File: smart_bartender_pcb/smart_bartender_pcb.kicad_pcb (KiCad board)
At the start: 2 copper layers, 105 x 60 mm, 8 parts, among them J1 Screw_Terminal_01x02, U1 AMS1117-5.0, U2 ULN2803A

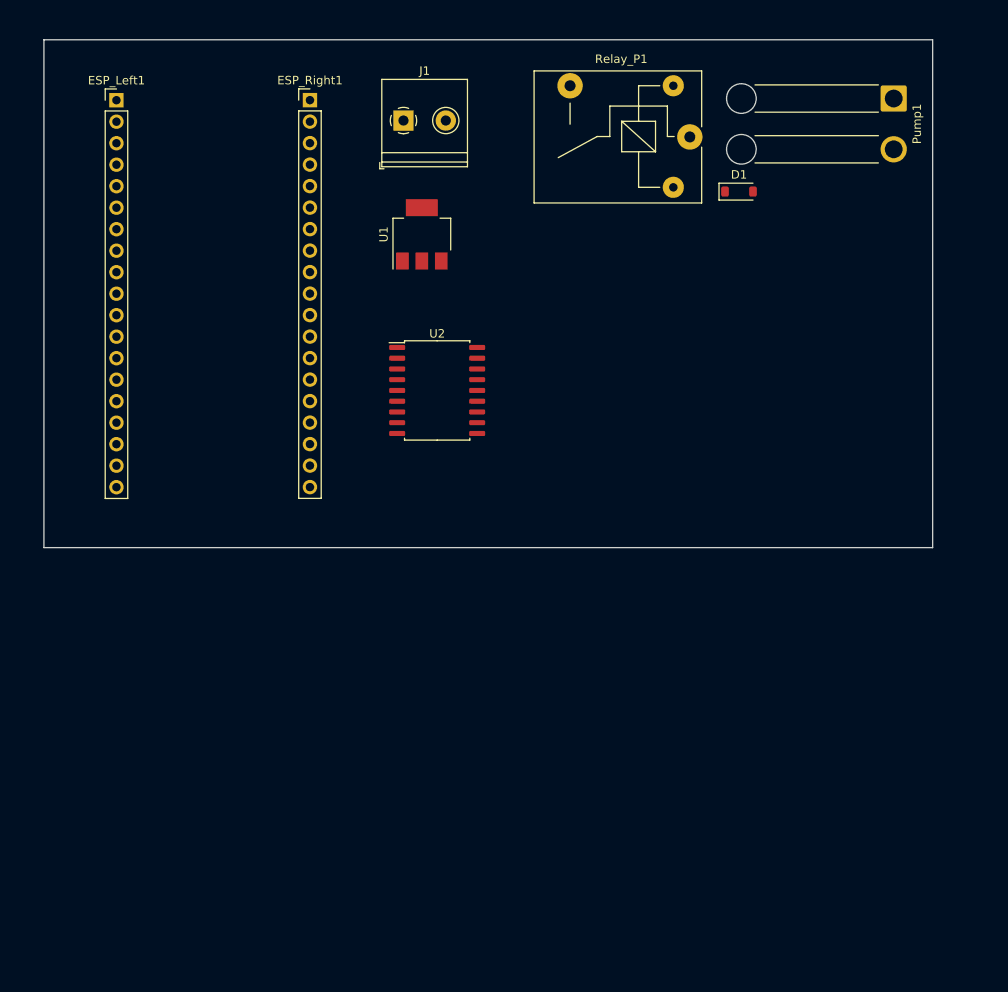
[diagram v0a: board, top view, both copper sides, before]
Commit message: started pcb layout
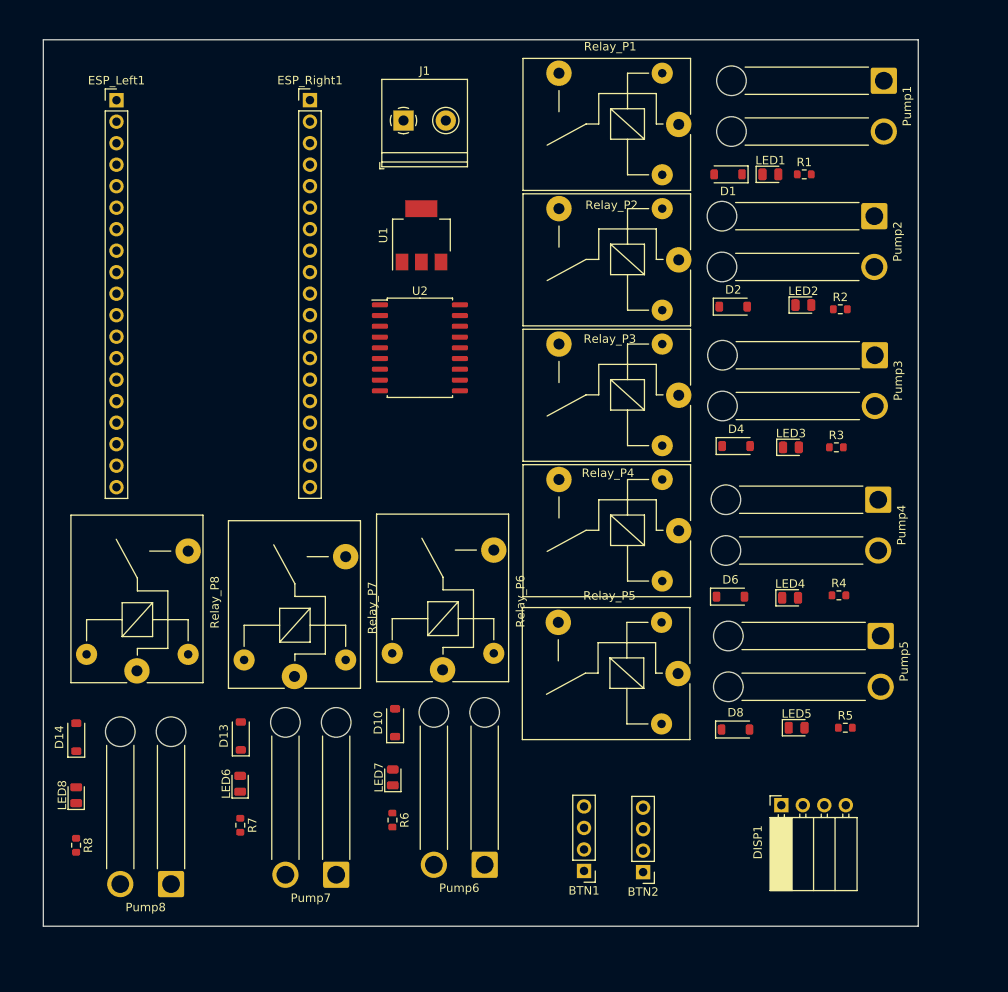
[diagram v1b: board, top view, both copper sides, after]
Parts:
- added BTN1: SW_Push_LED, Connector_PinHeader_2.54mm:PinHeader_1x04_P2.54mm_Vertical, F.Cu at (93.8, 118.2)
- added BTN2: SW_Push_LED, Connector_PinHeader_2.54mm:PinHeader_1x04_P2.54mm_Vertical, F.Cu at (100.8, 118.3)
- added D10: 1N4007, Diode_SMD:D_SOD-123, F.Cu at (71.5, 100.7)
- added D13: 1N4007, Diode_SMD:D_SOD-123, F.Cu at (53.3, 102.2)
- added D14: 1N4007, Diode_SMD:D_SOD-123, F.Cu at (33.8, 102.4)
- added D2: 1N4007, Diode_SMD:D_SOD-123, F.Cu at (111.4, 51.5)
- added D4: 1N4007, Diode_SMD:D_SOD-123, F.Cu at (111.8, 68.0)
- added D6: 1N4007, Diode_SMD:D_SOD-123, F.Cu at (111.1, 85.8)
- added D8: 1N4007, Diode_SMD:D_SOD-123, F.Cu at (111.7, 101.5)
- added DISP1: ~, Connector_PinSocket_2.54mm:PinSocket_1x04_P2.54mm_Horizontal, F.Cu at (117.1, 110.4)
- added LED1: LED, LED_SMD:LED_0805_2012Metric, F.Cu at (115.8, 35.9)
- added LED2: LED, LED_SMD:LED_0805_2012Metric, F.Cu at (119.7, 51.3)
- added LED3: LED, LED_SMD:LED_0805_2012Metric, F.Cu at (118.3, 68.2)
- added LED4: LED, LED_SMD:LED_0805_2012Metric, F.Cu at (118.2, 85.9)
- added LED5: LED, LED_SMD:LED_0805_2012Metric, F.Cu at (118.9, 101.3)
- added LED6: LED, LED_SMD:LED_0805_2012Metric, F.Cu at (53.2, 107.9)
- added LED7: LED, LED_SMD:LED_0805_2012Metric, F.Cu at (71.2, 107.2)
- added LED8: LED, LED_SMD:LED_0805_2012Metric, F.Cu at (33.8, 109.2)
- added Pump2: Conn_01x02_Socket, Connector_Wire:SolderWire-1.5sqmm_1x02_P6mm_D1.7mm_OD3mm_Relief, F.Cu at (128.1, 40.8)
- added Pump3: Conn_01x02_Socket, Connector_Wire:SolderWire-1.5sqmm_1x02_P6mm_D1.7mm_OD3mm_Relief, F.Cu at (128.2, 57.3)
- added Pump4: Conn_01x02_Socket, Connector_Wire:SolderWire-1.5sqmm_1x02_P6mm_D1.7mm_OD3mm_Relief, F.Cu at (128.6, 74.3)
- added Pump5: Conn_01x02_Socket, Connector_Wire:SolderWire-1.5sqmm_1x02_P6mm_D1.7mm_OD3mm_Relief, F.Cu at (128.9, 90.4)
- added Pump6: Conn_01x02_Socket, Connector_Wire:SolderWire-1.5sqmm_1x02_P6mm_D1.7mm_OD3mm_Relief, F.Cu at (82.1, 117.5)
- added Pump7: Conn_01x02_Socket, Connector_Wire:SolderWire-1.5sqmm_1x02_P6mm_D1.7mm_OD3mm_Relief, F.Cu at (64.5, 118.7)
- added Pump8: Conn_01x02_Socket, Connector_Wire:SolderWire-1.5sqmm_1x02_P6mm_D1.7mm_OD3mm_Relief, F.Cu at (45.0, 119.8)
- added R1: 110, Resistor_SMD:R_0603_1608Metric, F.Cu at (119.8, 35.9)
- added R2: 110, Resistor_SMD:R_0603_1608Metric, F.Cu at (124.1, 51.8)
- added R3: 110, Resistor_SMD:R_0603_1608Metric, F.Cu at (123.6, 68.2)
- added R4: 110, Resistor_SMD:R_0603_1608Metric, F.Cu at (123.9, 85.6)
- added R5: 110, Resistor_SMD:R_0603_1608Metric, F.Cu at (124.7, 101.3)
- added R6: 110, Resistor_SMD:R_0603_1608Metric, F.Cu at (71.2, 112.2)
- added R7: 110, Resistor_SMD:R_0603_1608Metric, F.Cu at (53.2, 112.8)
- added R8: 110, Resistor_SMD:R_0603_1608Metric, F.Cu at (33.8, 115.2)
- added Relay_P2: SANYOU_SRD_Form_A, Relay_THT:Relay_SPST_SANYOU_SRD_Series_Form_A, F.Cu at (105.0, 46.0)
- added Relay_P3: SANYOU_SRD_Form_A, Relay_THT:Relay_SPST_SANYOU_SRD_Series_Form_A, F.Cu at (105.0, 62.0)
- added Relay_P4: SANYOU_SRD_Form_A, Relay_THT:Relay_SPST_SANYOU_SRD_Series_Form_A, F.Cu at (105.0, 78.0)
- added Relay_P5: SANYOU_SRD_Form_A, Relay_THT:Relay_SPST_SANYOU_SRD_Series_Form_A, F.Cu at (104.9, 94.9)
- added Relay_P6: SANYOU_SRD_Form_A, Relay_THT:Relay_SPST_SANYOU_SRD_Series_Form_A, F.Cu at (77.1, 94.4)
- added Relay_P7: SANYOU_SRD_Form_A, Relay_THT:Relay_SPST_SANYOU_SRD_Series_Form_A, F.Cu at (59.6, 95.2)
- added Relay_P8: SANYOU_SRD_Form_A, Relay_THT:Relay_SPST_SANYOU_SRD_Series_Form_A, F.Cu at (41.0, 94.6)
- moved U2 5.44 mm to (74.4, 56.4)
- moved D1 2.41 mm to (110.8, 35.9), turned to 180 degrees
- moved Pump1 2.40 mm to (129.2, 24.8)
- moved Relay_P1 1.98 mm to (105.0, 30.0)
- moved U1 0.12 mm to (74.6, 43.1)
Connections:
- D1 pad 1: 5V -> 5V_P1
- D1 pad 2: 5V_P1 -> GND
- ESP_Left1 pad 10: unconnected-(ESP_Left1-P26-Pad10) -> BTN1
- ESP_Left1 pad 11: unconnected-(ESP_Left1-P27-Pad11) -> BTN2
- ESP_Left1 pad 9: unconnected-(ESP_Left1-P25-Pad9) -> P8
- ESP_Right1 pad 27: unconnected-(ESP_Right1-P16-Pad27) -> P1
- ESP_Right1 pad 28: unconnected-(ESP_Right1-P17-Pad28) -> P2
- ESP_Right1 pad 30: unconnected-(ESP_Right1-P18-Pad30) -> P3
- ESP_Right1 pad 31: unconnected-(ESP_Right1-P19-Pad31) -> P4
- ESP_Right1 pad 33: unconnected-(ESP_Right1-P21-Pad33) -> P5
- ESP_Right1 pad 36: unconnected-(ESP_Right1-P22-Pad36) -> P6
- ESP_Right1 pad 37: unconnected-(ESP_Right1-P23-Pad37) -> P7
- ESP_Right1 pad 38: unconnected-(ESP_Right1-GND-Pad38) -> GND
- Relay_P1 pad 2: 5V -> 5V_P1
- Relay_P1 pad 5: 5V_P1 -> GND
- U2 pad 10: GND -> 5V
- U2 pad 11: unconnected-(U2-O8-Pad11) -> 5V_P8
- U2 pad 12: unconnected-(U2-O7-Pad12) -> 5V_P7
- U2 pad 13: unconnected-(U2-O6-Pad13) -> 5V_P6
- U2 pad 14: unconnected-(U2-O5-Pad14) -> 5V_P5
- U2 pad 15: unconnected-(U2-O4-Pad15) -> 5V_P4
- U2 pad 16: unconnected-(U2-O3-Pad16) -> 5V_P3
- U2 pad 17: unconnected-(U2-O2-Pad17) -> 5V_P2
- U2 pad 2: unconnected-(U2-I2-Pad2) -> P2
- U2 pad 3: unconnected-(U2-I3-Pad3) -> P3
- U2 pad 4: unconnected-(U2-I4-Pad4) -> P4
- U2 pad 5: unconnected-(U2-I5-Pad5) -> P5
- U2 pad 6: unconnected-(U2-I6-Pad6) -> P6
- U2 pad 7: unconnected-(U2-I7-Pad7) -> P7
- U2 pad 8: unconnected-(U2-I8-Pad8) -> P8
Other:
- board size 105 x 60 mm -> 103.4 x 104.7 mm

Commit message: updated pcb
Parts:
- moved ESP_Left1 3.46 mm to (47.9, 47.3), turned to 180 degrees
- moved ESP_Right1 3.46 mm to (47.9, 47.3), turned to 180 degrees
- moved DISP1 3.40 mm to (114.0, 109.0)
- moved BTN1 1.72 mm to (93.8, 116.5)
- moved BTN2 1.72 mm to (100.8, 116.6)
- moved Pump2 1.27 mm to (126.8, 40.8)
- moved R2 1.27 mm to (122.8, 51.8)
- moved D8 1.27 mm to (110.4, 101.5)
- moved Pump5 1.27 mm to (127.6, 90.4)
- moved D4 1.27 mm to (110.5, 68.0)
- moved D6 1.27 mm to (109.8, 85.8)
- moved LED2 1.27 mm to (118.5, 51.3)
- moved LED3 1.27 mm to (117.0, 68.1)
- moved LED4 1.27 mm to (116.9, 85.9)
- moved LED5 1.27 mm to (117.7, 101.2)
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- renumbered Relay_P7 to Relay_P6, Relay_P6 to Relay_P7
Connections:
- DISP1 pad 1: unconnected-(DISP1-3V3-Pad1) -> 3V3
- DISP1 pad 2: unconnected-(DISP1-SDA-Pad2) -> SDA
- DISP1 pad 3: unconnected-(DISP1-SCL-Pad3) -> SCL
- DISP1 pad 4: unconnected-(DISP1-GND-Pad4) -> GND
- ESP_Left1 pad 1: unconnected-(ESP_Left1-3V3-Pad1) -> 3V3
- ESP_Left1 pad 10: BTN1 -> P7
- ESP_Left1 pad 11: BTN2 -> P8
- ESP_Left1 pad 7: unconnected-(ESP_Left1-P32-Pad7) -> BTN1
- ESP_Left1 pad 8: unconnected-(ESP_Left1-P33-Pad8) -> BTN2
- ESP_Left1 pad 9: P8 -> P6
- ESP_Right1 pad 33: P5 -> SDA
- ESP_Right1 pad 36: P6 -> SCL
- ESP_Right1 pad 37: P7 -> P5
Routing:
- net 12V: track 0.00 -> 165.0 mm, vias 0 -> 1
- net SCL: track 0.00 -> 105.7 mm
- net SDA: track 0.00 -> 102.0 mm
- net BTN2: track 0.00 -> 81.1 mm
- net BTN1: track 0.00 -> 74.1 mm
- net 5V_P8: track 0.00 -> 73.1 mm, vias 0 -> 1
- net 3V3: track 0.00 -> 70.8 mm
- net 5V_P5: track 0.00 -> 68.3 mm
- net 5V_P6: track 0.00 -> 63.5 mm, vias 0 -> 1
- net 5V_P7: track 0.00 -> 57.7 mm, vias 0 -> 1
- net 5V_P4: track 0.00 -> 57.4 mm
- net 5V_P1: track 0.00 -> 54.8 mm
- net 5V_P2: track 0.00 -> 53.0 mm
- net 5V_P3: track 0.00 -> 49.4 mm
- net P5: track 0.00 -> 49.4 mm
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- added copper zone on B.Cu, net GND
- added copper zone on F.Cu, net GND
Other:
- board size 103.4 x 104.7 mm -> 100 x 100 mm
